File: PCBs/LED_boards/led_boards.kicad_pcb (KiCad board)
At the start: 2 copper layers, 14 parts, among them J1 from_shield, J2 from_shield

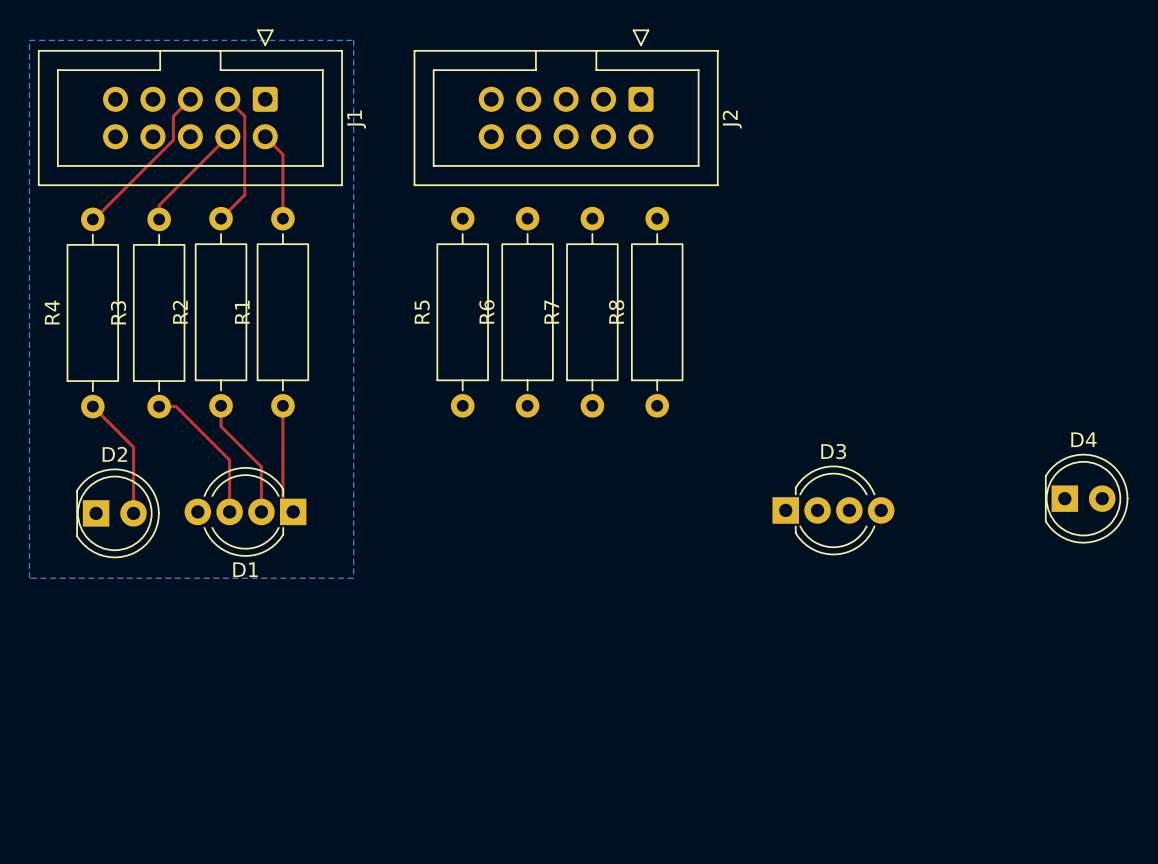
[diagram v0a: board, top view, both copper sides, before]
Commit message: update bom and finish first version of PCBs
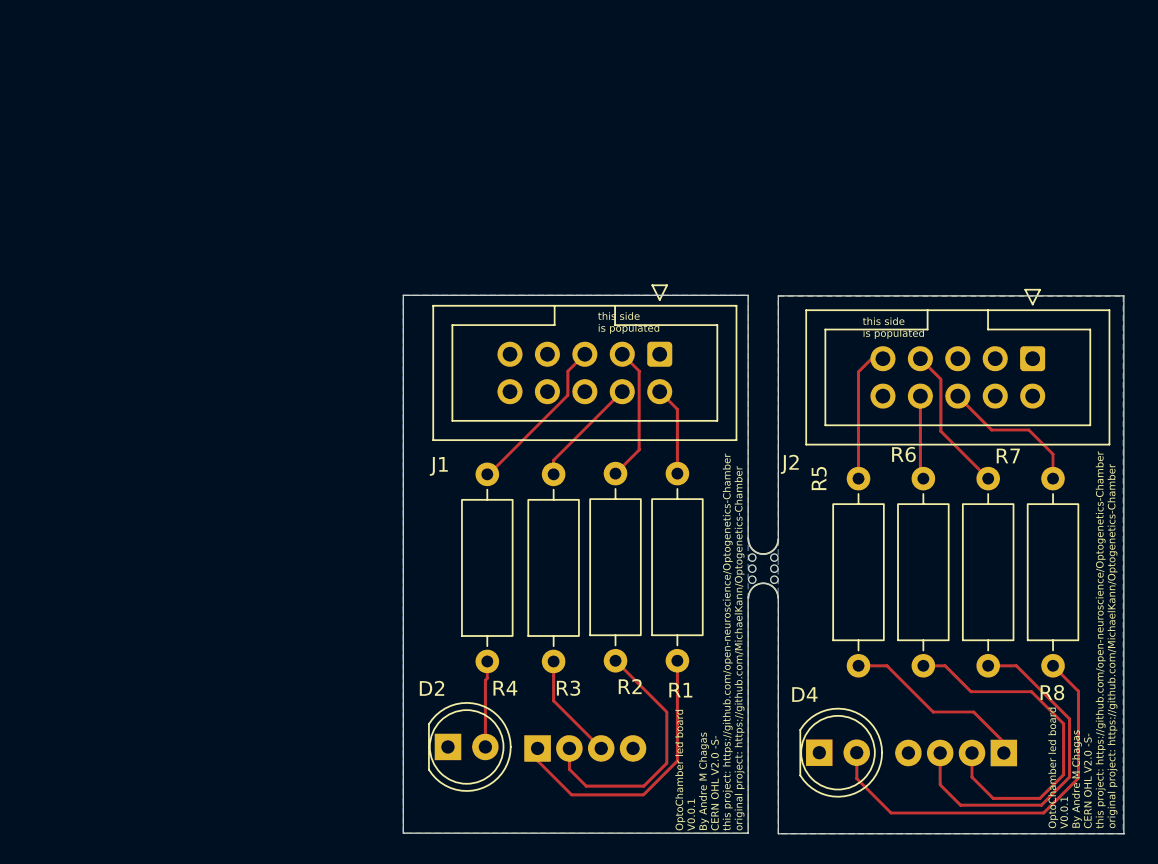
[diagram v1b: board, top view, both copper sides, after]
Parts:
- added mouse-bite-2mm-slot: VAL**, Panelization:mouse-bite-2mm-slot, F.Cu at (148.3, 67.3)
- D1, D3: moved to B.Cu
- moved R7 32.1 mm to (163.6, 73.9)
- moved R8 32.1 mm to (168.0, 73.9)
- moved R5 32.1 mm to (154.8, 73.9)
- moved R6 32.1 mm to (159.2, 73.9)
- moved J2 31.9 mm to (166.6, 53.1)
- moved J1 31.9 mm to (141.3, 52.8)
- moved R2 31.9 mm to (138.3, 73.6)
- moved R3 31.9 mm to (134.1, 73.7)
- moved R4 31.9 mm to (129.6, 73.7)
- moved R1 31.9 mm to (142.5, 73.6)
- moved D2 28.7 mm to (126.9, 79.5)
- moved D4 24.0 mm to (152.1, 79.8)
- moved D1 23.1 mm to (133.0, 79.5), turned to 0 degrees
- moved D3 22.1 mm to (164.6, 79.9), turned to 180 degrees
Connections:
- D2 pad 1: unconnected-(D2-K-Pad1) -> GND
- D4 pad 1: unconnected-(D4-K-Pad1) -> GND
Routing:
- net Net-(D4-A): track 0.00 -> 27.1 mm
- net Net-(D3-GA): track 0.00 -> 23.7 mm
- net Net-(D3-BA): track 0.00 -> 23.3 mm
- net Net-(D3-RA): track 0.00 -> 12.7 mm
- net Net-(D1-RA): track 7.49 -> 19.0 mm
- net Net-(J2-Pin_7): track 0.00 -> 10.0 mm
- net Net-(J2-Pin_6): track 0.00 -> 9.75 mm
- net Net-(J2-Pin_9): track 0.00 -> 9.27 mm
- net Net-(D1-GA): track 8.34 -> 17.5 mm
- net Net-(J2-Pin_8): track 0.00 -> 5.68 mm
- net Net-(D1-BA): track 9.80 -> 7.24 mm
- net Net-(D2-A): track 8.39 -> 5.85 mm
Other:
- board outline added: 48.9 x 36.5 mm
- board text added: "OptoChamber led board V0.0.1 By Andre M Chagas CERN OHL V2.0 -S- this project: https://github.com/open-neuroscience/Optogenetics-Chamber original project: https://github.com/MichaelKann/Optogenetics-Chamber"
- board text added: "this side is populated"
